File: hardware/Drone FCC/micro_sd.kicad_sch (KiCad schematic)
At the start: 9 parts, among them J15 DM3AT-SF-PEJM5

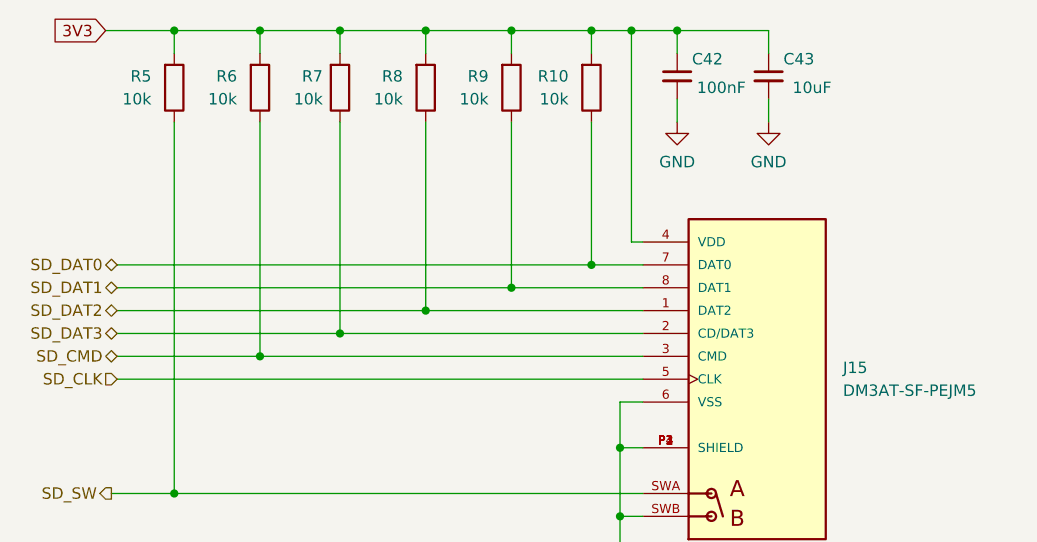
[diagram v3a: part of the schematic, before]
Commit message: re enumeration of components
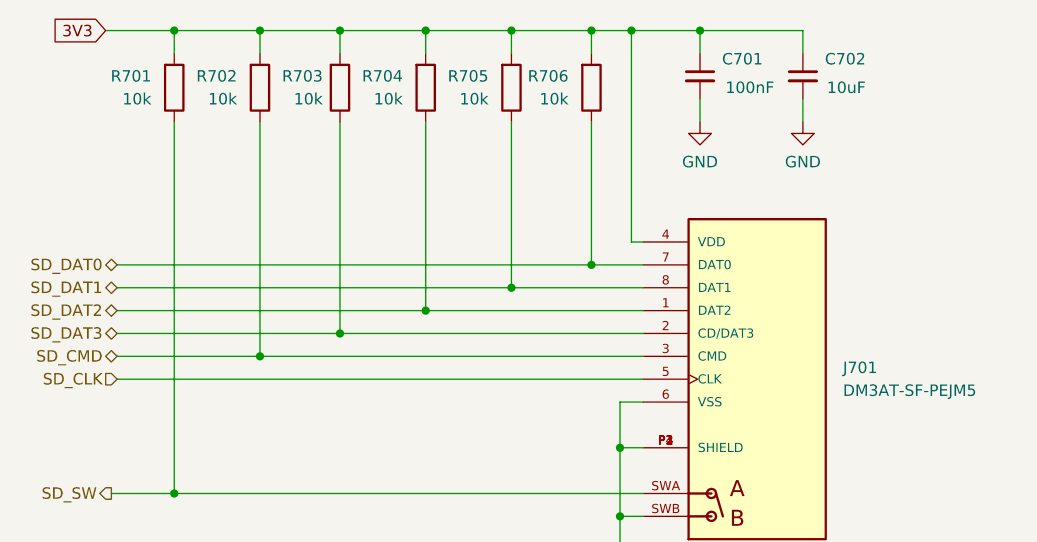
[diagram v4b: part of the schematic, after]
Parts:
- renumbered C42 to C701, C43 to C702, J15 to J701, R5 to R701, R6 to R702, R7 to R703, R8 to R704, R9 to R705, R10 to R706
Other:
- moved on the sheet: C701, C702
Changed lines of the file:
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@@
   (junction (at 153.035 72.39) (diameter 0) (color 0 0 0 0)
   )
-  (junction (at 162.56 72.39) (diameter 0) (color 0 0 0 0)
+  (junction (at 165.1 72.39) (diameter 0) (color 0 0 0 0)
   )
   (junction (at 134.62 103.505) (diameter 0) (color 0 0 0 0)
@@
     (stroke (width 0) (type default) (color 0 0 0 0))
   )
+  (wire (pts (xy 165.1 72.39) (xy 176.53 72.39))
+    (stroke (width 0) (type default) (color 0 0 0 0))
+  )
   (wire (pts (xy 144.145 82.55) (xy 144.145 100.965))
     (stroke (width 0) (type default) (color 0 0 0 0))
@@
     (stroke (width 0) (type default) (color 0 0 0 0))
   )
-  (wire (pts (xy 162.56 72.39) (xy 157.48 72.39))
+  (wire (pts (xy 157.48 72.39) (xy 165.1 72.39))
     (stroke (width 0) (type default) (color 0 0 0 0))
   )
@@
     (stroke (width 0) (type default) (color 0 0 0 0))
   )
-  (wire (pts (xy 172.72 72.39) (xy 162.56 72.39))
-    (stroke (width 0) (type default) (color 0 0 0 0))
-  )
   (wire (pts (xy 100.33 98.425) (xy 153.035 98.425))
     (stroke (width 0) (type default) (color 0 0 0 0))
   )
-  (wire (pts (xy 162.56 74.93) (xy 162.56 72.39))
+  (wire (pts (xy 165.1 74.93) (xy 165.1 72.39))
     (stroke (width 0) (type default) (color 0 0 0 0))
   )
@@
     (stroke (width 0) (type default) (color 0 0 0 0))
   )
-  (wire (pts (xy 172.72 80.01) (xy 172.72 82.55))
+  (wire (pts (xy 176.53 80.01) (xy 176.53 82.55))
     (stroke (width 0) (type default) (color 0 0 0 0))
   )
@@
     (stroke (width 0) (type default) (color 0 0 0 0))
   )
-  (wire (pts (xy 162.56 80.01) (xy 162.56 82.55))
+  (wire (pts (xy 165.1 80.01) (xy 165.1 82.55))
     (stroke (width 0) (type default) (color 0 0 0 0))
   )
@@
     (stroke (width 0) (type default) (color 0 0 0 0))
   )
-  (wire (pts (xy 172.72 74.93) (xy 172.72 72.39))
+  (wire (pts (xy 176.53 74.93) (xy 176.53 72.39))
     (stroke (width 0) (type default) (color 0 0 0 0))
   )
@@
     (pin "1")
   )
-  (symbol (lib_id "power:GND") (at 162.56 82.55 0) (unit 1)
-    (in_bom yes) (on_board yes) (fields_autoplaced)
-    (property "Reference" "#PWR0142" (id 0) (at 162.56 88.9 0)
-      (effects (font (size 1.27 1.27)) hide)
-    )
-    (property "Value" "GND" (id 1) (at 162.56 86.995 0))
-    (property "Footprint" "" (id 2) (at 162.56 82.55 0)
-      (effects (font (size 1.27 1.27)) hide)
-    )
-    (property "Datasheet" "" (id 3) (at 162.56 82.55 0)
-      (effects (font (size 1.27 1.27)) hide)
-    )
-    (pin "1")
-  )
-  (symbol (lib_id "Device:C_Small") (at 162.56 77.47 0) (unit 1)
+  (symbol (lib_id "power:GND") (at 165.1 82.55 0) (unit 1)
+    (in_bom yes) (on_board yes) (fields_autoplaced)
+    (property "Reference" "#PWR0142" (id 0) (at 165.1 88.9 0)
+      (effects (font (size 1.27 1.27)) hide)
+    )
+    (property "Value" "GND" (id 1) (at 165.1 86.995 0))
+    (property "Footprint" "" (id 2) (at 165.1 82.55 0)
+      (effects (font (size 1.27 1.27)) hide)
+    )
+    (property "Datasheet" "" (id 3) (at 165.1 82.55 0)
+      (effects (font (size 1.27 1.27)) hide)
+    )
+    (pin "1")
+  )
+  (symbol (lib_id "Device:C_Small") (at 165.1 77.47 0) (unit 1)
     (in_bom yes) (on_board yes)
-    (property "Reference" "C42" (id 0) (at 167.64 75.565 0)
-      (effects (font (size 1.27 1.27)) (justify right))
-    )
-    (property "Value" "100nF" (id 1) (at 170.18 78.74 0)
-      (effects (font (size 1.27 1.27)) (justify right))
-    )
-    (property "Footprint" "" (id 2) (at 162.56 77.47 0)
-      (effects (font (size 1.27 1.27)) hide)
-    )
-    (property "Datasheet" "~" (id 3) (at 162.56 77.47 0)
+    (property "Reference" "C701" (id 0) (at 172.085 75.565 0)
+      (effects (font (size 1.27 1.27)) (justify right))
+    )
+    (property "Value" "100nF" (id 1) (at 173.355 78.74 0)
+      (effects (font (size 1.27 1.27)) (justify right))
+    )
+    (property "Footprint" "" (id 2) (at 165.1 77.47 0)
+      (effects (font (size 1.27 1.27)) hide)
+    )
+    (property "Datasheet" "~" (id 3) (at 165.1 77.47 0)
       (effects (font (size 1.27 1.27)) hide)
     )
@@
   (symbol (lib_id "DM3AT-SF-PEJM5:DM3AT-SF-PEJM5") (at 171.45 111.125 0) (unit 1)
     (in_bom yes) (on_board yes) (fields_autoplaced)
-    (property "Reference" "J15" (id 0) (at 180.975 109.8549 0)
+    (property "Reference" "J701" (id 0) (at 180.975 109.8549 0)
       (effects (font (size 1.27 1.27)) (justify left))
     )
@@
   (symbol (lib_id "Device:R") (at 134.62 78.74 0) (mirror x) (unit 1)
     (in_bom yes) (on_board yes) (fields_autoplaced)
-    (property "Reference" "R8" (id 0) (at 132.08 77.4699 0)
+    (property "Reference" "R704" (id 0) (at 132.08 77.4699 0)
       (effects (font (size 1.27 1.27)) (justify right))
     )
@@
   (symbol (lib_id "Device:R") (at 144.145 78.74 0) (mirror x) (unit 1)
     (in_bom yes) (on_board yes) (fields_autoplaced)
-    (property "Reference" "R9" (id 0) (at 141.605 77.4699 0)
+    (property "Reference" "R705" (id 0) (at 141.605 77.4699 0)
       (effects (font (size 1.27 1.27)) (justify right))
     )
@@
     (pin "2")
   )
-  (symbol (lib_id "power:GND") (at 172.72 82.55 0) (unit 1)
-    (in_bom yes) (on_board yes) (fields_autoplaced)
-    (property "Reference" "#PWR0143" (id 0) (at 172.72 88.9 0)
-      (effects (font (size 1.27 1.27)) hide)
-    )
-    (property "Value" "GND" (id 1) (at 172.72 86.995 0))
-    (property "Footprint" "" (id 2) (at 172.72 82.55 0)
-      (effects (font (size 1.27 1.27)) hide)
-    )
-    (property "Datasheet" "" (id 3) (at 172.72 82.55 0)
+  (symbol (lib_id "power:GND") (at 176.53 82.55 0) (unit 1)
+    (in_bom yes) (on_board yes) (fields_autoplaced)
+    (property "Reference" "#PWR0143" (id 0) (at 176.53 88.9 0)
+      (effects (font (size 1.27 1.27)) hide)
+    )
+    (property "Value" "GND" (id 1) (at 176.53 86.995 0))
+    (property "Footprint" "" (id 2) (at 176.53 82.55 0)
+      (effects (font (size 1.27 1.27)) hide)
+    )
+    (property "Datasheet" "" (id 3) (at 176.53 82.55 0)
       (effects (font (size 1.27 1.27)) hide)
     )
@@
   (symbol (lib_id "Device:R") (at 125.095 78.74 0) (mirror x) (unit 1)
     (in_bom yes) (on_board yes) (fields_autoplaced)
-    (property "Reference" "R7" (id 0) (at 123.19 77.4699 0)
+    (property "Reference" "R703" (id 0) (at 123.19 77.4699 0)
       (effects (font (size 1.27 1.27)) (justify right))
     )
@@
   (symbol (lib_id "Device:R") (at 106.68 78.74 0) (mirror x) (unit 1)
     (in_bom yes) (on_board yes) (fields_autoplaced)
-    (property "Reference" "R5" (id 0) (at 104.14 77.4699 0)
+    (property "Reference" "R701" (id 0) (at 104.14 77.4699 0)
       (effects (font (size 1.27 1.27)) (justify right))
     )
@@
   (symbol (lib_id "Device:R") (at 116.205 78.74 0) (mirror x) (unit 1)
     (in_bom yes) (on_board yes) (fields_autoplaced)
-    (property "Reference" "R6" (id 0) (at 113.665 77.4699 0)
+    (property "Reference" "R702" (id 0) (at 113.665 77.4699 0)
       (effects (font (size 1.27 1.27)) (justify right))
     )
@@
     (pin "2")
   )
-  (symbol (lib_id "Device:C_Small") (at 172.72 77.47 0) (unit 1)
+  (symbol (lib_id "Device:C_Small") (at 176.53 77.47 0) (unit 1)
     (in_bom yes) (on_board yes)
-    (property "Reference" "C43" (id 0) (at 177.8 75.565 0)
-      (effects (font (size 1.27 1.27)) (justify right))
-    )
-    (property "Value" "10uF" (id 1) (at 179.705 78.74 0)
-      (effects (font (size 1.27 1.27)) (justify right))
-    )
-    (property "Footprint" "" (id 2) (at 172.72 77.47 0)
-      (effects (font (size 1.27 1.27)) hide)
-    )
-    (property "Datasheet" "~" (id 3) (at 172.72 77.47 0)
+    (property "Reference" "C702" (id 0) (at 183.515 75.565 0)
+      (effects (font (size 1.27 1.27)) (justify right))
+    )
+    (property "Value" "10uF" (id 1) (at 183.515 78.74 0)
+      (effects (font (size 1.27 1.27)) (justify right))
+    )
+    (property "Footprint" "" (id 2) (at 176.53 77.47 0)
+      (effects (font (size 1.27 1.27)) hide)
+    )
+    (property "Datasheet" "~" (id 3) (at 176.53 77.47 0)
       (effects (font (size 1.27 1.27)) hide)
     )
@@
   (symbol (lib_id "Device:R") (at 153.035 78.74 0) (mirror x) (unit 1)
     (in_bom yes) (on_board yes) (fields_autoplaced)
-    (property "Reference" "R10" (id 0) (at 150.495 77.4699 0)
-      (effects (font (size 1.27 1.27)) (justify right))
-    )
+    (property "Reference" "R706" (id 0) (at 150.495 77.4699 0)
+      (effects (font (size 1.27 1.27)) (justify right))
+    )

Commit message: start routing
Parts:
- C701, C702: footprint (none) -> Capacitor_SMD:C_0603_1608Metric_Pad1.08x0.95mm_HandSolder
- R701, R702, R703, R704, R705, R706: footprint (none) -> Resistor_SMD:R_0402_1005Metric_Pad0.72x0.64mm_HandSolder
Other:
- note added: "En el layout, hay que forzar que cuando se inserta la tarjeta SD, su capacitor de entrada se carga utilizando los capacitores de desacople C701 y C702."
- note added: "Este capacitor tiene que tener una ESR que no sea baja, 2 ó 3 Ohms está bien."
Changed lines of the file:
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@@
+    (stroke (width 0) (type default) (color 0 0 0 0))
+  )
+  (polyline (pts (xy 173.99 69.85) (xy 173.99 88.9))
     (stroke (width 0) (type default) (color 0 0 0 0))
   )
@@
     (stroke (width 0) (type default) (color 0 0 0 0))
   )
+  (polyline (pts (xy 173.99 69.85) (xy 195.58 69.85))
+    (stroke (width 0) (type default) (color 0 0 0 0))
+  )
   (wire (pts (xy 100.33 103.505) (xy 134.62 103.505))
     (stroke (width 0) (type default) (color 0 0 0 0))
@@
     (stroke (width 0) (type default) (color 0 0 0 0))
   )
+  (polyline (pts (xy 173.99 88.9) (xy 195.58 88.9))
+    (stroke (width 0) (type default) (color 0 0 0 0))
+  )
   (wire (pts (xy 100.33 98.425) (xy 153.035 98.425))
     (stroke (width 0) (type default) (color 0 0 0 0))
@@
     (stroke (width 0) (type default) (color 0 0 0 0))
   )
+  (polyline (pts (xy 195.58 88.9) (xy 195.58 69.85))
+    (stroke (width 0) (type default) (color 0 0 0 0))
+  )
   (wire (pts (xy 106.68 82.55) (xy 106.68 123.825))
     (stroke (width 0) (type default) (color 0 0 0 0))
@@
   (wire (pts (xy 134.62 82.55) (xy 134.62 103.505))
     (stroke (width 0) (type default) (color 0 0 0 0))
+  )
+  (text "En el layout, hay que forzar que cuando\nse inserta la tarjeta SD, su capacitor\nde entrada se carga utilizando los \ncapacitores de desacople C701 y C702."
+    (at 180.34 102.235 0)
+    (effects (font (size 1.27 1.27)) (justify left bottom))
+  )
+  (text "Este capacitor tiene que tener una\nESR que no sea baja, 2 ó 3 Ohms\nestá bien."
+    (at 173.99 69.215 0)
+    (effects (font (size 1.27 1.27)) (justify left bottom))
   )
   (global_label "3V3" (shape input) (at 99.06 72.39 180) (fields_autoplaced)
@@
       (effects (font (size 1.27 1.27)) (justify right))
     )
-    (property "Footprint" "" (id 2) (at 165.1 77.47 0)
+    (property "Footprint" "Capacitor_SMD:C_0603_1608Metric_Pad1.08x0.95mm_HandSolder" (id 2) (at 165.1 77.47 0)
       (effects (font (size 1.27 1.27)) hide)
     )
@@
       (effects (font (size 1.27 1.27)) (justify right))
     )
-    (property "Footprint" "" (id 2) (at 132.842 78.74 90)
+    (property "Footprint" "Resistor_SMD:R_0402_1005Metric_Pad0.72x0.64mm_HandSolder" (id 2) (at 132.842 78.74 90)
       (effects (font (size 1.27 1.27)) hide)
     )
@@
       (effects (font (size 1.27 1.27)) (justify right))
     )
-    (property "Footprint" "" (id 2) (at 142.367 78.74 90)
+    (property "Footprint" "Resistor_SMD:R_0402_1005Metric_Pad0.72x0.64mm_HandSolder" (id 2) (at 142.367 78.74 90)
       (effects (font (size 1.27 1.27)) hide)
     )
@@
       (effects (font (size 1.27 1.27)) (justify right))
     )
-    (property "Footprint" "" (id 2) (at 123.317 78.74 90)
+    (property "Footprint" "Resistor_SMD:R_0402_1005Metric_Pad0.72x0.64mm_HandSolder" (id 2) (at 123.317 78.74 90)
       (effects (font (size 1.27 1.27)) hide)
     )
@@
       (effects (font (size 1.27 1.27)) (justify right))
     )
-    (property "Footprint" "" (id 2) (at 104.902 78.74 90)
+    (property "Footprint" "Resistor_SMD:R_0402_1005Metric_Pad0.72x0.64mm_HandSolder" (id 2) (at 104.902 78.74 90)
       (effects (font (size 1.27 1.27)) hide)
     )
@@
       (effects (font (size 1.27 1.27)) (justify right))
     )
-    (property "Footprint" "" (id 2) (at 114.427 78.74 90)
+    (property "Footprint" "Resistor_SMD:R_0402_1005Metric_Pad0.72x0.64mm_HandSolder" (id 2) (at 114.427 78.74 90)
       (effects (font (size 1.27 1.27)) hide)
     )
@@
       (effects (font (size 1.27 1.27)) (justify right))
     )
-    (property "Footprint" "" (id 2) (at 176.53 77.47 0)
+    (property "Footprint" "Capacitor_SMD:C_0603_1608Metric_Pad1.08x0.95mm_HandSolder" (id 2) (at 176.53 77.47 0)
       (effects (font (size 1.27 1.27)) hide)
     )
@@
       (effects (font (size 1.27 1.27)) (justify right))
     )
-    (property "Footprint" "" (id 2) (at 151.257 78.74 90)
-      (effects (font (size 1.27 1.27)) hide)
-    )
+    (property "Footprint" "Resistor_SMD:R_0402_1005Metric_Pad0.72x0.64mm_HandSolder" (id 2) (at 151.257 78.74 90)
+      (effects (font (size 1.27 1.27)) hide)
+    )

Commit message: positioning of componentes 80x80 pcb
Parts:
- C701: footprint Capacitor_SMD:C_0603_1608Metric_Pad1.08x0.95mm_HandSolder -> Capacitor_SMD:C_0402_1005Metric_Pad0.74x0.62mm_HandSolder
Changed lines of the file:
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@@
       (effects (font (size 1.27 1.27)) (justify right))
     )
-    (property "Footprint" "Capacitor_SMD:C_0603_1608Metric_Pad1.08x0.95mm_HandSolder" (id 2) (at 165.1 77.47 0)
+    (property "Footprint" "Capacitor_SMD:C_0402_1005Metric_Pad0.74x0.62mm_HandSolder" (id 2) (at 165.1 77.47 0)
       (effects (font (size 1.27 1.27)) hide)
     )

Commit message: finish SD routing
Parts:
- added C703, C704, C705, C706, C707: 100nF, Capacitor_SMD:C_0402_1005Metric_Pad0.74x0.62mm_HandSolder, symbol Device:C_Small
- added R707, R708, R709, R710, R711, R712: 50, Resistor_SMD:R_0402_1005Metric_Pad0.72x0.64mm_HandSolder, symbol Device:R
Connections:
- net 3V3: now also C703.1, C704.1, C705.1, C706.1, C707.1
- net GND: now also C703.2, C704.2, C705.2, C706.2, C707.2
- net SD_CLK: now also R712.2; no longer J701.5 (CLK)
- net SD_CMD: now also R711.2; no longer J701.3 (CMD)
- net SD_DAT0: now also R707.2; no longer J701.7 (DAT0)
- net SD_DAT1: now also R708.2; no longer J701.8 (DAT1)
- net SD_DAT2: now also R709.2; no longer J701.1 (DAT2)
- net SD_DAT3: now also R710.2; no longer J701.2 (CD/DAT3)
- new net: J701.7 (DAT0), R707.1
- new net: J701.1 (DAT2), R709.1
- new net: J701.2 (CD/DAT3), R710.1
- new net: J701.3 (CMD), R711.1
- new net: J701.5 (CLK), R712.1
- new net: J701.8 (DAT1), R708.1
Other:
- note added: "Resistores en serie para adaptación de impedancias. Deben estar aproximadamente en el medio del camino de pista para lograr su función."
- moved on the sheet: R701, R702, R703, R704, R705, R706

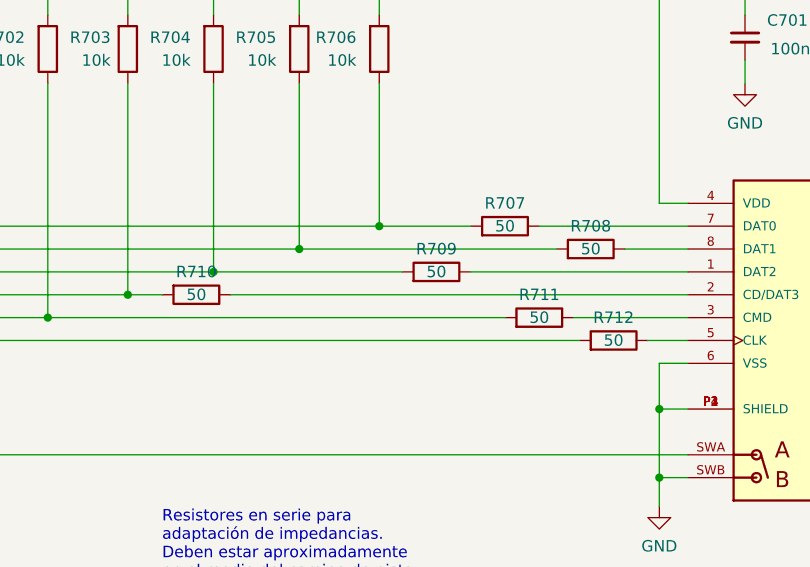
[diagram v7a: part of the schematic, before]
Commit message: set values of resistors for LEDs
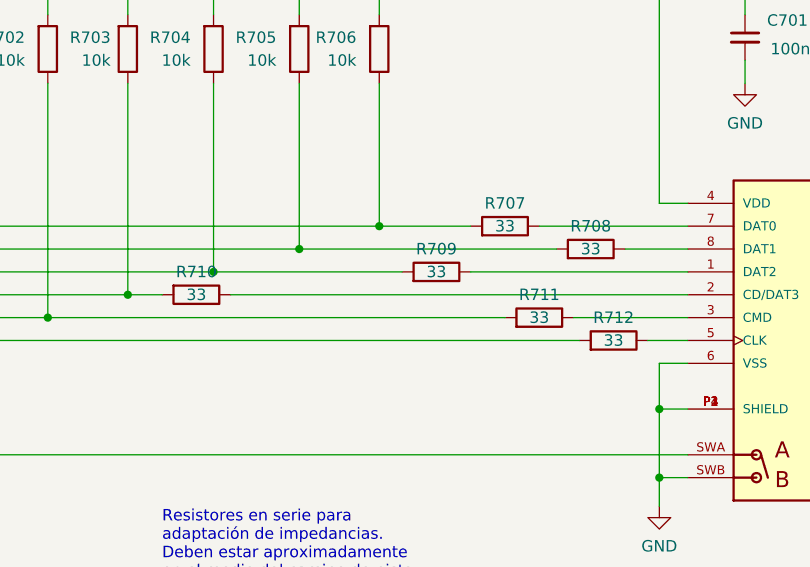
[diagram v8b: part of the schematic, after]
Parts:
- R707, R708, R709, R710, R711, R712: value 50 -> 33
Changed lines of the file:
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@@
     (in_bom yes) (on_board yes)
     (property "Reference" "R707" (id 0) (at 138.43 95.885 90))
-    (property "Value" "50" (id 1) (at 138.43 98.425 90))
+    (property "Value" "33" (id 1) (at 138.43 98.425 90))
     (property "Footprint" "Resistor_SMD:R_0402_1005Metric_Pad0.72x0.64mm_HandSolder" (id 2) (at 138.43 100.203 90)
       (effects (font (size 1.27 1.27)) hide)
@@
     (in_bom yes) (on_board yes)
     (property "Reference" "R711" (id 0) (at 142.24 106.045 90))
-    (property "Value" "50" (id 1) (at 142.24 108.585 90))
+    (property "Value" "33" (id 1) (at 142.24 108.585 90))
     (property "Footprint" "Resistor_SMD:R_0402_1005Metric_Pad0.72x0.64mm_HandSolder" (id 2) (at 142.24 110.363 90)
       (effects (font (size 1.27 1.27)) hide)
@@
     (in_bom yes) (on_board yes)
     (property "Reference" "R709" (id 0) (at 130.81 100.965 90))
-    (property "Value" "50" (id 1) (at 130.81 103.505 90))
+    (property "Value" "33" (id 1) (at 130.81 103.505 90))
     (property "Footprint" "Resistor_SMD:R_0402_1005Metric_Pad0.72x0.64mm_HandSolder" (id 2) (at 130.81 105.283 90)
       (effects (font (size 1.27 1.27)) hide)
@@
     (in_bom yes) (on_board yes)
     (property "Reference" "R710" (id 0) (at 104.14 103.505 90))
-    (property "Value" "50" (id 1) (at 104.14 106.045 90))
+    (property "Value" "33" (id 1) (at 104.14 106.045 90))
     (property "Footprint" "Resistor_SMD:R_0402_1005Metric_Pad0.72x0.64mm_HandSolder" (id 2) (at 104.14 104.267 90)
       (effects (font (size 1.27 1.27)) hide)
@@
     (in_bom yes) (on_board yes)
     (property "Reference" "R708" (id 0) (at 147.955 98.425 90))
-    (property "Value" "50" (id 1) (at 147.955 100.965 90))
+    (property "Value" "33" (id 1) (at 147.955 100.965 90))
     (property "Footprint" "Resistor_SMD:R_0402_1005Metric_Pad0.72x0.64mm_HandSolder" (id 2) (at 147.955 102.743 90)
       (effects (font (size 1.27 1.27)) hide)
@@
     (in_bom yes) (on_board yes)
     (property "Reference" "R712" (id 0) (at 150.495 108.585 90))
-    (property "Value" "50" (id 1) (at 150.495 111.125 90))
+    (property "Value" "33" (id 1) (at 150.495 111.125 90))
     (property "Footprint" "Resistor_SMD:R_0402_1005Metric_Pad0.72x0.64mm_HandSolder" (id 2) (at 150.495 112.903 90)
       (effects (font (size 1.27 1.27)) hide)
